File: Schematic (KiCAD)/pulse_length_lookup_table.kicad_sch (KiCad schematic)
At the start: 121 parts

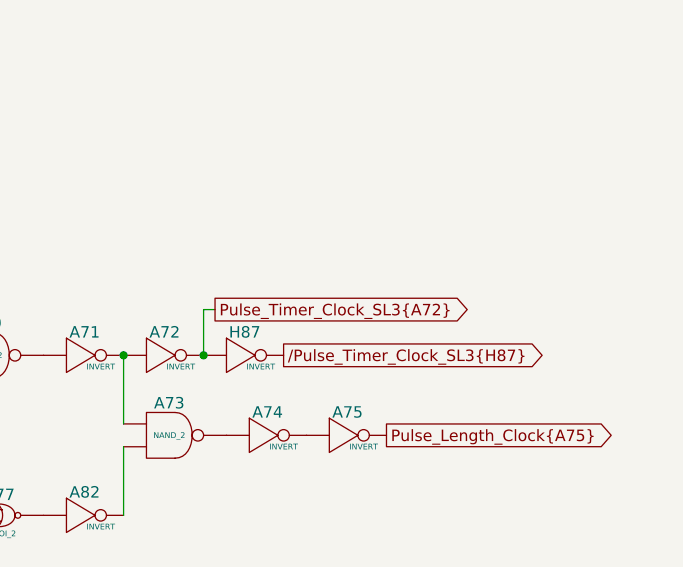
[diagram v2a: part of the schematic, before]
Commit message: - All cells in the left and center areas have now been added into the schematics.  - Changed naming of the PDF files; I was accidentally writing over furrtek's original with my new PDF.
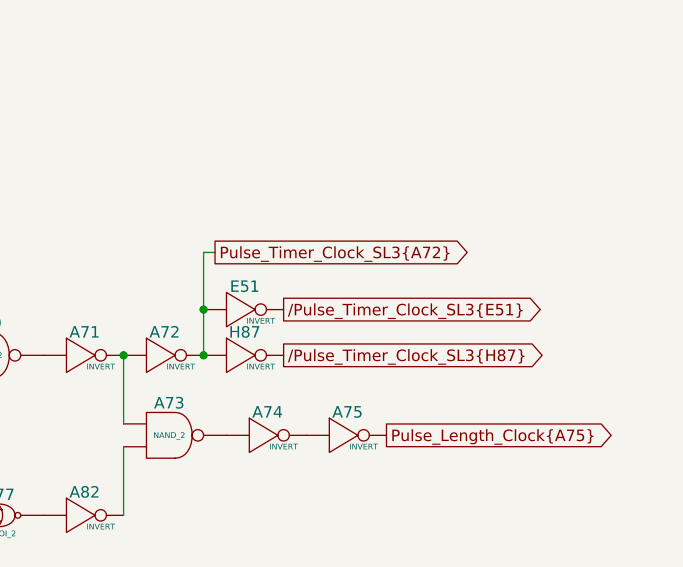
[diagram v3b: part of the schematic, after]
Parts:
- added E51: INVERT, symbol MMC5:INVERT
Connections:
- net Pulse_Timer_Clock_SL3{A72}: now also E51. (X)
- net at B108. (X): now also A78. (X); no longer A70. (X)
- net at A71. (X): now also A72. (X), A73. (X); no longer A70. (X)
- net at C16. (X): now also D47. (X); no longer C15. (X)
- net at D45. (X): now also D46. (X); no longer C16. (X)
- net at D47. (X): now also D48. (X); no longer C16. (X)
- net at D72. (X): now also C22. (X); no longer D71. (X)
- net at D92. (X): now also C26. (X); no longer D91. (X)
- net at C26. (X): now also C25. (X); no longer D92. (X)
- net at C18. (X): now also D51. (X); no longer C17. (X)
- net at D106. (X): now also C28. (X); no longer D105. (X)
- net at A58. (X): now also A57. (X), A66. (/Q7); no longer A59. (X)
- net at D66. (X): now also D65. (X); no longer C20. (X)
- net at A67. (/Q4): now also A65. (X)
- net at A66.7. (X): now also A66.4. (X); no longer A67. (/Q4)
- net at A68. (X): now also A66.4. (X); no longer A67. (/Q4)
- net at A66.6. (X): now also A66.4. (X); no longer A67. (/Q4)
- net at A69. (X): now also A77. (X); no longer A67. (/Q4)
- net at A65. (X): now also A64. (X); no longer A67. (/Q4)
- net at A66.4. (X): now also A66.5. (X), A78. (X); no longer A66.7. (X)
- net at D64. (X): now also C20. (X); no longer D63. (X)
- net at D76. (X): now also C22. (X); no longer D75. (X)
- net at D53. (X): now also C18. (X); no longer D54. (X)
- net at D96. (X): now also D95. (X); no longer C26. (X)
- net at A73. (X): now also A74. (X); no longer A82. (X)
- net at A74. (X): now also A75. (X); no longer A73. (X)
- net at D49. (X): now also C18. (X); no longer D50. (X)
- net at D55. (X): now also C18. (X); no longer D56. (X)
- net at D74. (X): now also D73. (X); no longer C22. (X)
- net at D70. (X): now also D69. (X); no longer C22. (X)
- net at D68. (X): now also D67. (X); no longer C22. (X)
- net at A77. (X): now also A82. (X); no longer A81. (X)
- net at A77. (X), A80. (X): now also A79. (X)
- net at D104. (X): now also C28. (X); no longer D103. (X)
- net at C28. (X): now also C27. (X); no longer D104. (X)
- net at D58. (X): now also C20. (X); no longer D57. (X)
- net at C20. (X): now also D62. (X); no longer D58. (X)
- net at A66.3. (X): now also A66. (/Q7); no longer A66.4. (X)
- net at D78. (X): now also C24. (X); no longer D77. (X)
- net at C24. (X): now also D88. (X); no longer D78. (X)
- net at D102. (X): now also C28. (X); no longer D101. (X)
- net at D51. (X): now also D52. (X); no longer C18. (X)
- net at D100. (X): now also C26. (X); no longer D99. (X)
- net at D60. (X): now also C20. (X); no longer D59. (X)
- net at D84. (X): now also D83. (X); no longer C24. (X)
- net at D86. (X): now also C24. (X); no longer D85. (X)
- net at D82. (X): now also D81. (X); no longer C24. (X)
- net at D80. (X): now also D79. (X); no longer C24. (X)
- net at D90. (X): now also C26. (X); no longer D89. (X)
- net at A66.2. (X): now also A66. (/Q7); no longer A66.5. (X)
- net at A60. (X): now also A56. (X); no longer A61. (X)
- net at D94. (X): now also C26. (X); no longer D93. (X)
- net at D98. (X): now also D97. (X); no longer C26. (X)
- new net: A70. (X), B108. (X)
- new net: A70. (X), A71. (X)
- new net: C15. (X), C16. (X)
- new net: C16. (X), D45. (X)
- new net: D71. (X), D72. (X)
- new net: D91. (X), D92. (X)
- new net: C17. (X), C18. (X)
- new net: D105. (X), D106. (X)
- new net: A58. (X), A59. (X)
- new net: C20. (X), D66. (X)
- new net: A66.7. (X), A67. (/Q4)
- new net: A67. (/Q4), A68. (X)
- new net: A66.6. (X), A67. (/Q4)
- new net: A67. (/Q4), A69. (X)
- new net: A66. (/Q7), A67. (/Q4)
- new net: D63. (X), D64. (X)
- new net: D75. (X), D76. (X)
- new net: D53. (X), D54. (X)
- new net: C26. (X), D96. (X)
- new net: A73. (X), A82. (X)
- new net: D49. (X), D50. (X)
- new net: A64. (X), A66.4. (X), A66.5. (X)
- new net: D55. (X), D56. (X)
- new net: C21. (X), C22. (X)
- new net: C22. (X), D74. (X)
- new net: C22. (X), D70. (X)
- new net: C22. (X), D68. (X)
- new net: A77. (X), A81. (X)
- new net: A77. (X), A80. (X)
- new net: D103. (X), D104. (X)
- new net: D57. (X), D58. (X)
- new net: D61. (X), D62. (X)
- new net: A66.3. (X), A66.4. (X)
- new net: D77. (X), D78. (X)
- new net: C23. (X), C24. (X)
- new net: C19. (X), C20. (X)
- new net: A55. (/Q), A56. (X), A57. (X)
- new net: B43. (X), B44. (X)
- new net: B42. (X), B43. (X)
- new net: D101. (X), D102. (X)
- new net: C10. (X), D38. (Ripple_Out)
- new net: C10. (X), C9. (X)
- new net: D100. (X), D99. (X)
- new net: D59. (X), D60. (X)
- new net: D38. (Ripple_Out), D39. (Ripple_Out)
- new net: C24. (X), D84. (X)
- new net: D85. (X), D86. (X)
- new net: C11. (Ripple_Out), C12. (Ripple_Out)
- new net: B42. (X), C11. (Ripple_Out)
- new net: D87. (X), D88. (X)
- new net: C24. (X), D82. (X)
- new net: C24. (X), D80. (X)
- new net: D89. (X), D90. (X)
- new net: A66.2. (X), A66.5. (X)
- new net: C8. (X), C9. (X)
- new net: A60. (X), A61. (X)
- new net: D93. (X), D94. (X)
- new net: A78. (X), A83. (X), B107. (X)
- new net: C26. (X), D98. (X)
- new net /Pulse_Timer_Clock_SL3{E51}: E51. (X)
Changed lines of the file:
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@@
 	)
 	(junction
+		(at 337.82 205.74)
+		(diameter 0)
+		(color 0 0 0 0)
+	)
+	(junction
 		(at 227.33 199.39)
 		(diameter 0)
@@
 	(wire
 		(pts
+			(xy 337.82 205.74) (xy 337.82 210.82)
+		)
+		(stroke
+			(width 0)
+			(type default)
+		)
+	)
+	(wire
+		(pts
 			(xy 146.05 77.47) (xy 146.05 62.23)
 		)
@@
 	(wire
 		(pts
-			(xy 337.82 205.74) (xy 337.82 210.82)
+			(xy 337.82 199.39) (xy 337.82 205.74)
 		)
 		(stroke
@@
 	(wire
 		(pts
-			(xy 339.09 205.74) (xy 337.82 205.74)
+			(xy 339.09 199.39) (xy 337.82 199.39)
 		)
 		(stroke
@@
 	(global_label "Pulse_Timer_Clock_SL3{A72}"
 		(shape output)
-		(at 339.09 205.74 0)
+		(at 339.09 199.39 0)
 		(fields_autoplaced yes)
 		(effects
@@
 		)
 		(property "Intersheetrefs" "${INTERSHEET_REFS}"
-			(at 369.1684 205.74 0)
+			(at 369.1684 199.39 0)
 			(effects
 				(font
@@
 		)
 	)
+	(global_label "{slash}Pulse_Timer_Clock_SL3{E51}"
+		(shape output)
+		(at 346.71 205.74 0)
+		(fields_autoplaced yes)
+		(effects
+			(font
+				(size 1.27 1.27)
+			)
+			(justify left)
+		)
+		(property "Intersheetrefs" "${INTERSHEET_REFS}"
+			(at 378.1793 205.74 0)
+			(effects
+				(font
+					(size 1.27 1.27)
+				)
+				(justify left)
+				(hide yes)
+			)
+		)
+	)
 	(global_label "{slash}CPU_D7{E59}"
 		(shape input)
@@
 					(unit 1)
 				)
+			)
+		)
+	)
+	(symbol
+		(lib_name "INVERT_63")
+		(lib_id "MMC5:INVERT")
+		(at 342.9 205.74 0)
+		(unit 1)
+		(exclude_from_sim no)
+		(in_bom yes)
+		(on_board yes)
+		(dnp no)
+		(fields_autoplaced yes)
+		(property "Reference" "E51"
+			(at 342.392 202.438 0)
+			(do_not_autoplace yes)
+			(effects
+				(font
+					(size 1.27 1.27)
+				)
+				(justify top)
+			)
+		)
+		(property "Value" "INVERT"
+			(at 344.17 207.01 0)
+			(do_not_autoplace yes)
+			(effects
+				(font
+					(size 0.635 0.635)
+				)
+			)
+		)
+		(property "Footprint" ""
+			(at 342.9 205.74 0)
+			(effects
+				(font
+					(size 1.27 1.27)
+				)
+				(hide yes)
+			)
+		)
+		(property "Datasheet" ""
+			(at 342.9 205.74 0)
+			(effects
+				(font
+					(size 1.27 1.27)
+				)
+				(hide yes)
+			)
+		)
+		(property "Description" ""
+			(at 342.9 205.74 0)
+			(effects
+				(font
+					(size 1.27 1.27)
+				)
+				(hide yes)
+			)
+		)
+		(pin ""
+		)
+		(pin ""
+		)
+		(instances
+			(project "MMC5"
+				(path "/46093bf6-f83e-4237-9ece-7350a682aff0/c1262e85-2c8c-4550-8b9b-35681710fa23"
+					(reference "E51")
+					(unit 1)
+				)
